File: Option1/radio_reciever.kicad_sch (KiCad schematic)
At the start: 13 parts, among them J3 Conn_01x05_Pin, J4 Conn_01x04_Pin, J5 Conn_01x05_Pin, SW401 4*4*1.7

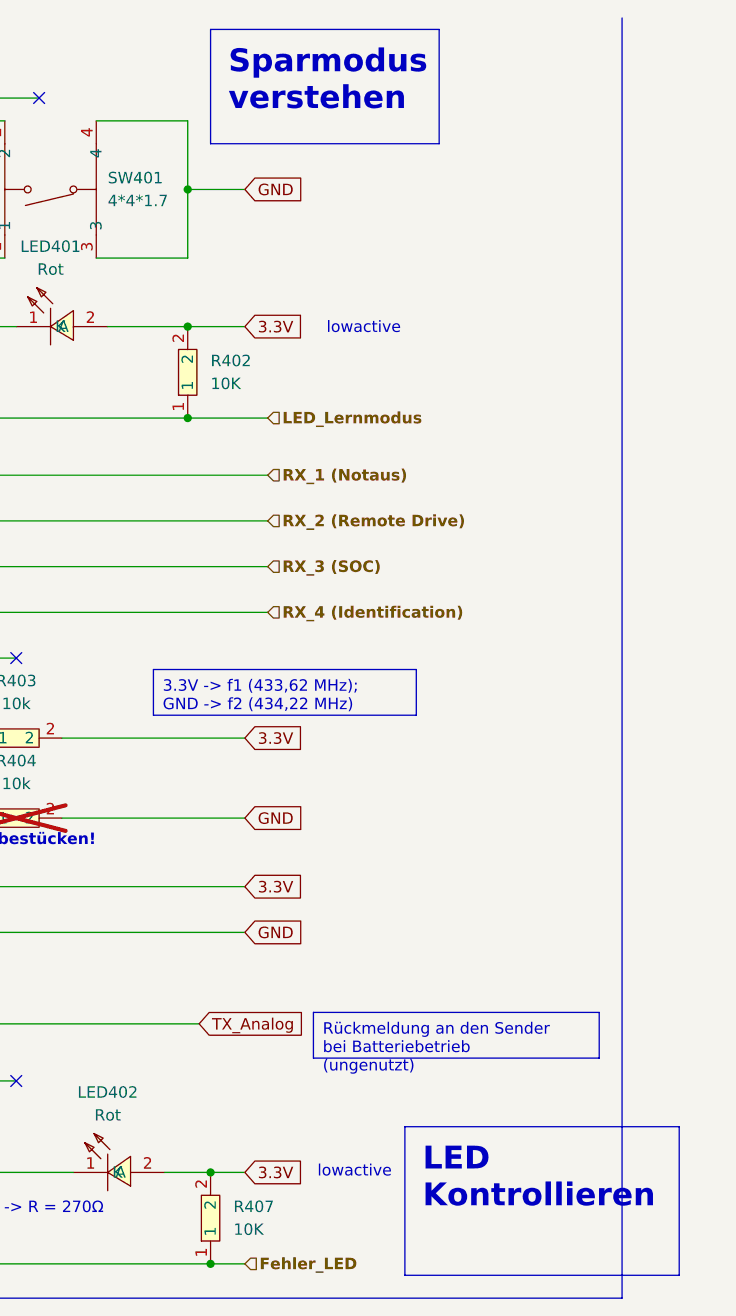
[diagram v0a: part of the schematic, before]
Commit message: SPI Flash hinzugefügt, IN/Outputs vereinheitlicht, USB Flash Möglichkeit hinzugefügt, Display fehtl noch
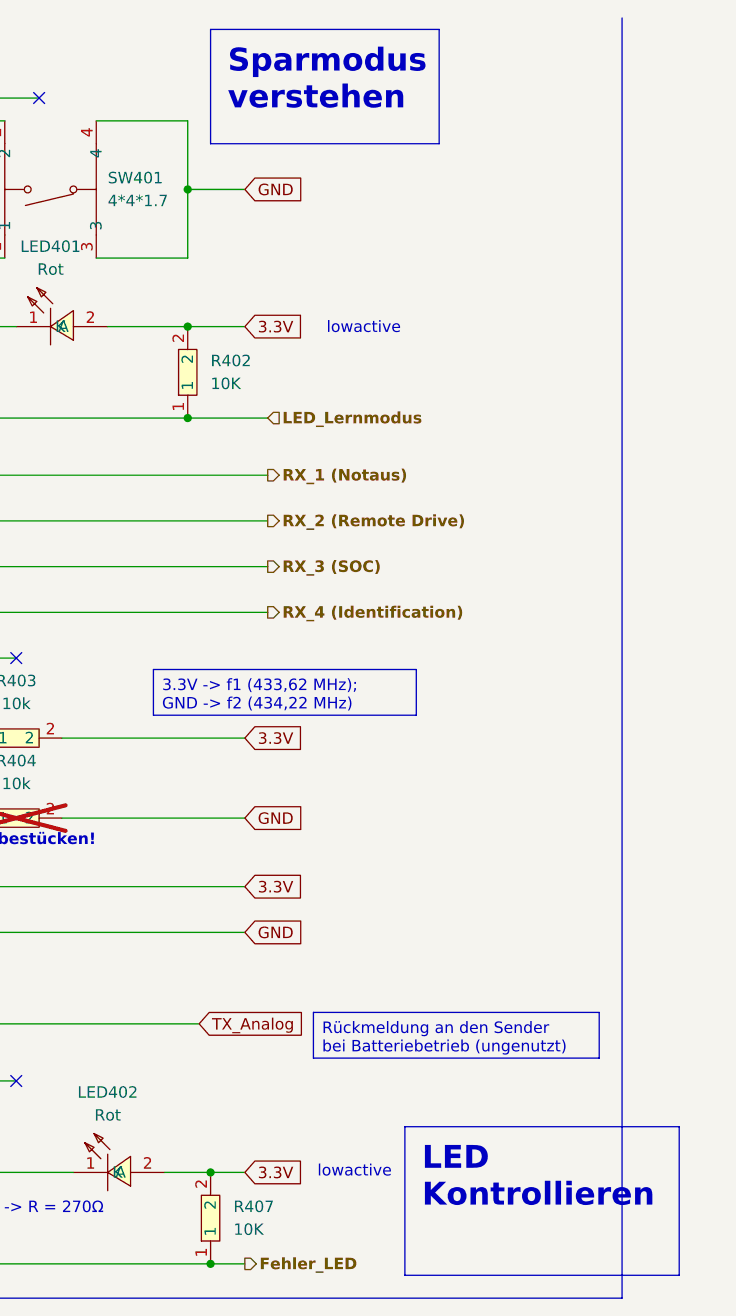
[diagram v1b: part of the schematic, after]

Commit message: Erste issues eingearbeitet
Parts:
- removed LED401, LED402: Rot, easyeda2kicad:LED0603-RD, symbol easyeda2kicad:KT-0603R
- removed R401, R406: 270, easyeda2kicad:R0603, symbol easyeda2kicad:0603WAF2700T5E
- added LED_Error, LED_Learn: XL-1608SYGC-06, easyeda2kicad:LED0603-RD_GREEN, symbol EasyEda2KiCad:XL-1608SYGC-06
- added R401, R406: 220Ω, easyeda2kicad:R0603, symbol EasyEda2KiCad:0603WAJ0221T5E
- R404: now left out of the parts list
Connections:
- net 3.3V: now also LED_Error.2 (A), LED_Learn.2 (A)
- net Fehler_LED: now also R406.1
- net LED_Modus: now also R401.1
- new net: LED_Learn.1 (K), R401.2
- new net: LED_Error.1 (K), R406.2
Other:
- note added: "I_LED = 5mA"
- note removed: "I_LED = 5mA -> R = 270Ω"

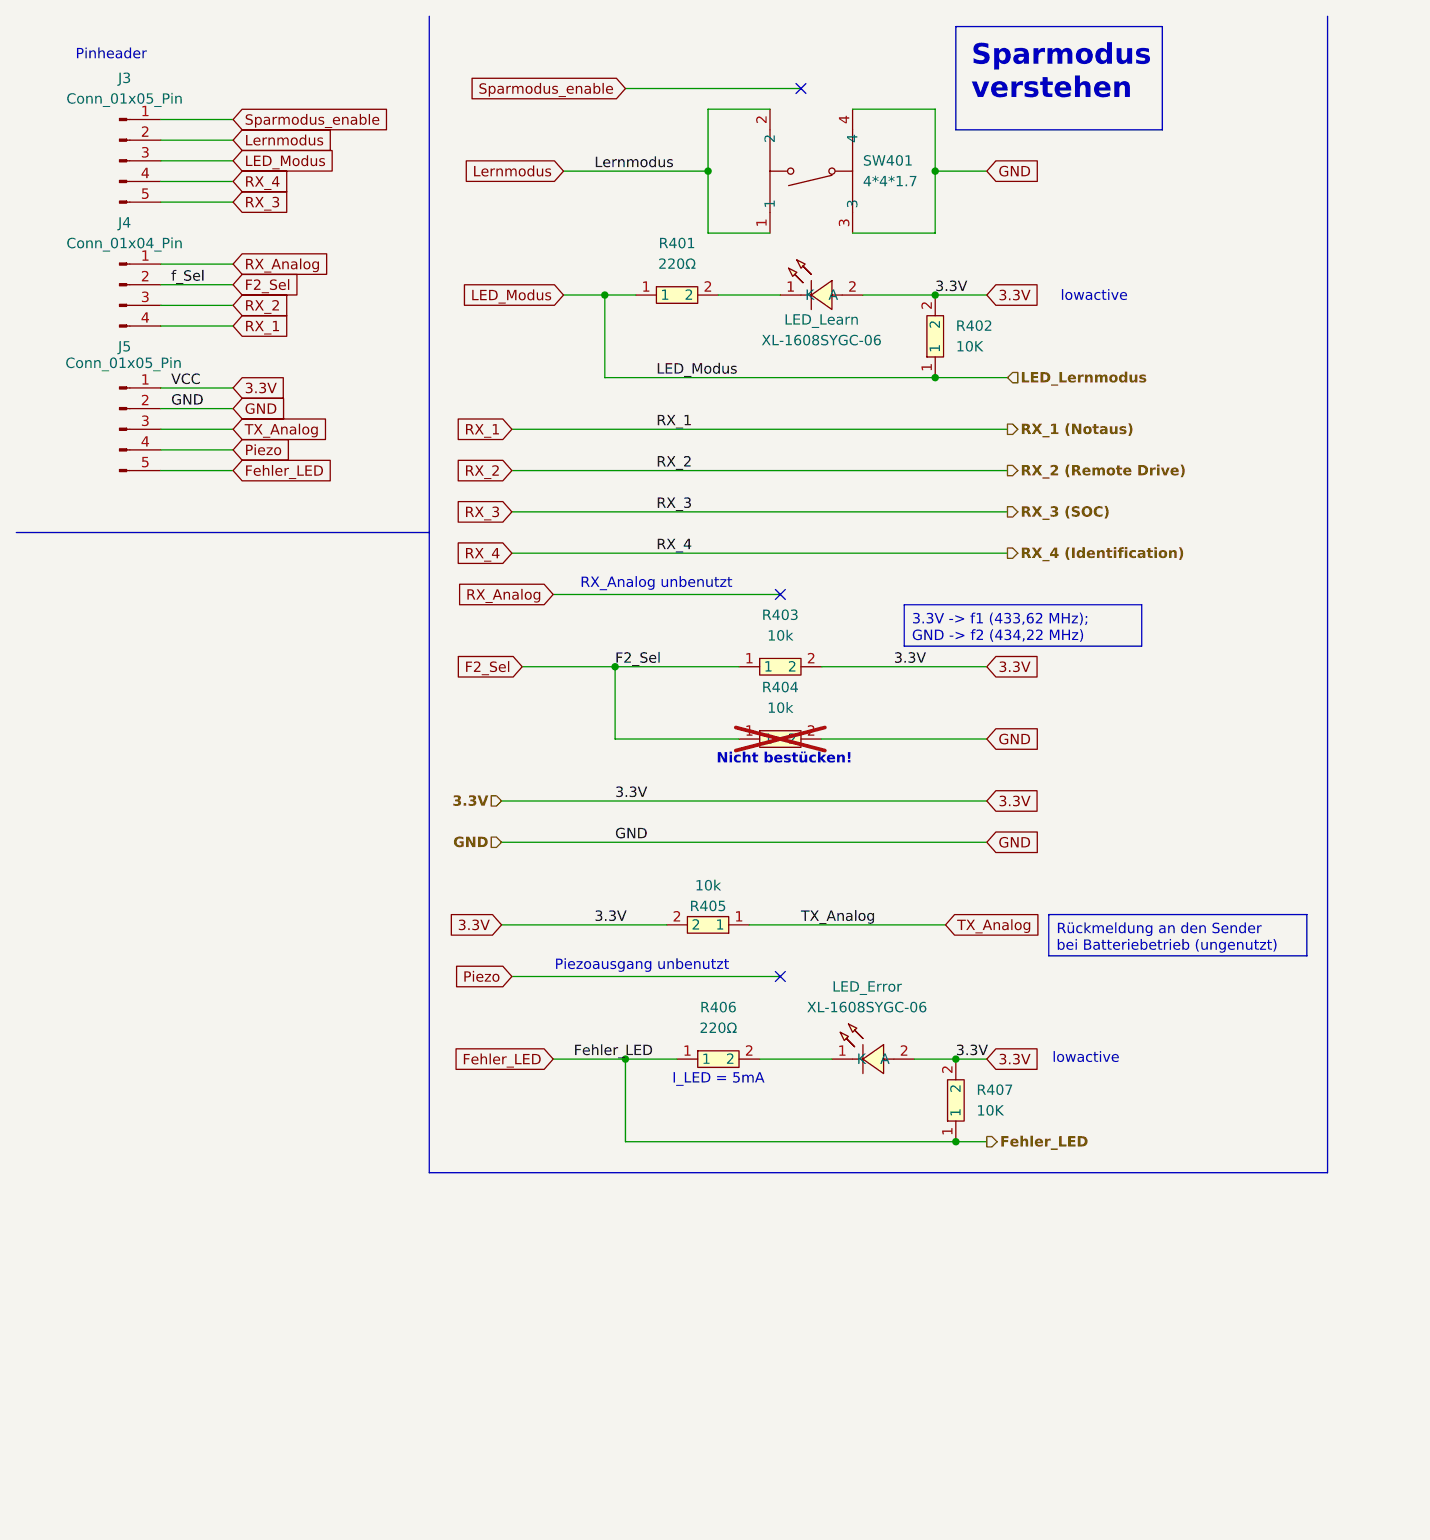
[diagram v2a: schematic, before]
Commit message: USB Schaltung angepasst, Transistoren korrigiert, Stecker ausgetauscht, Dioden hinzugefügt
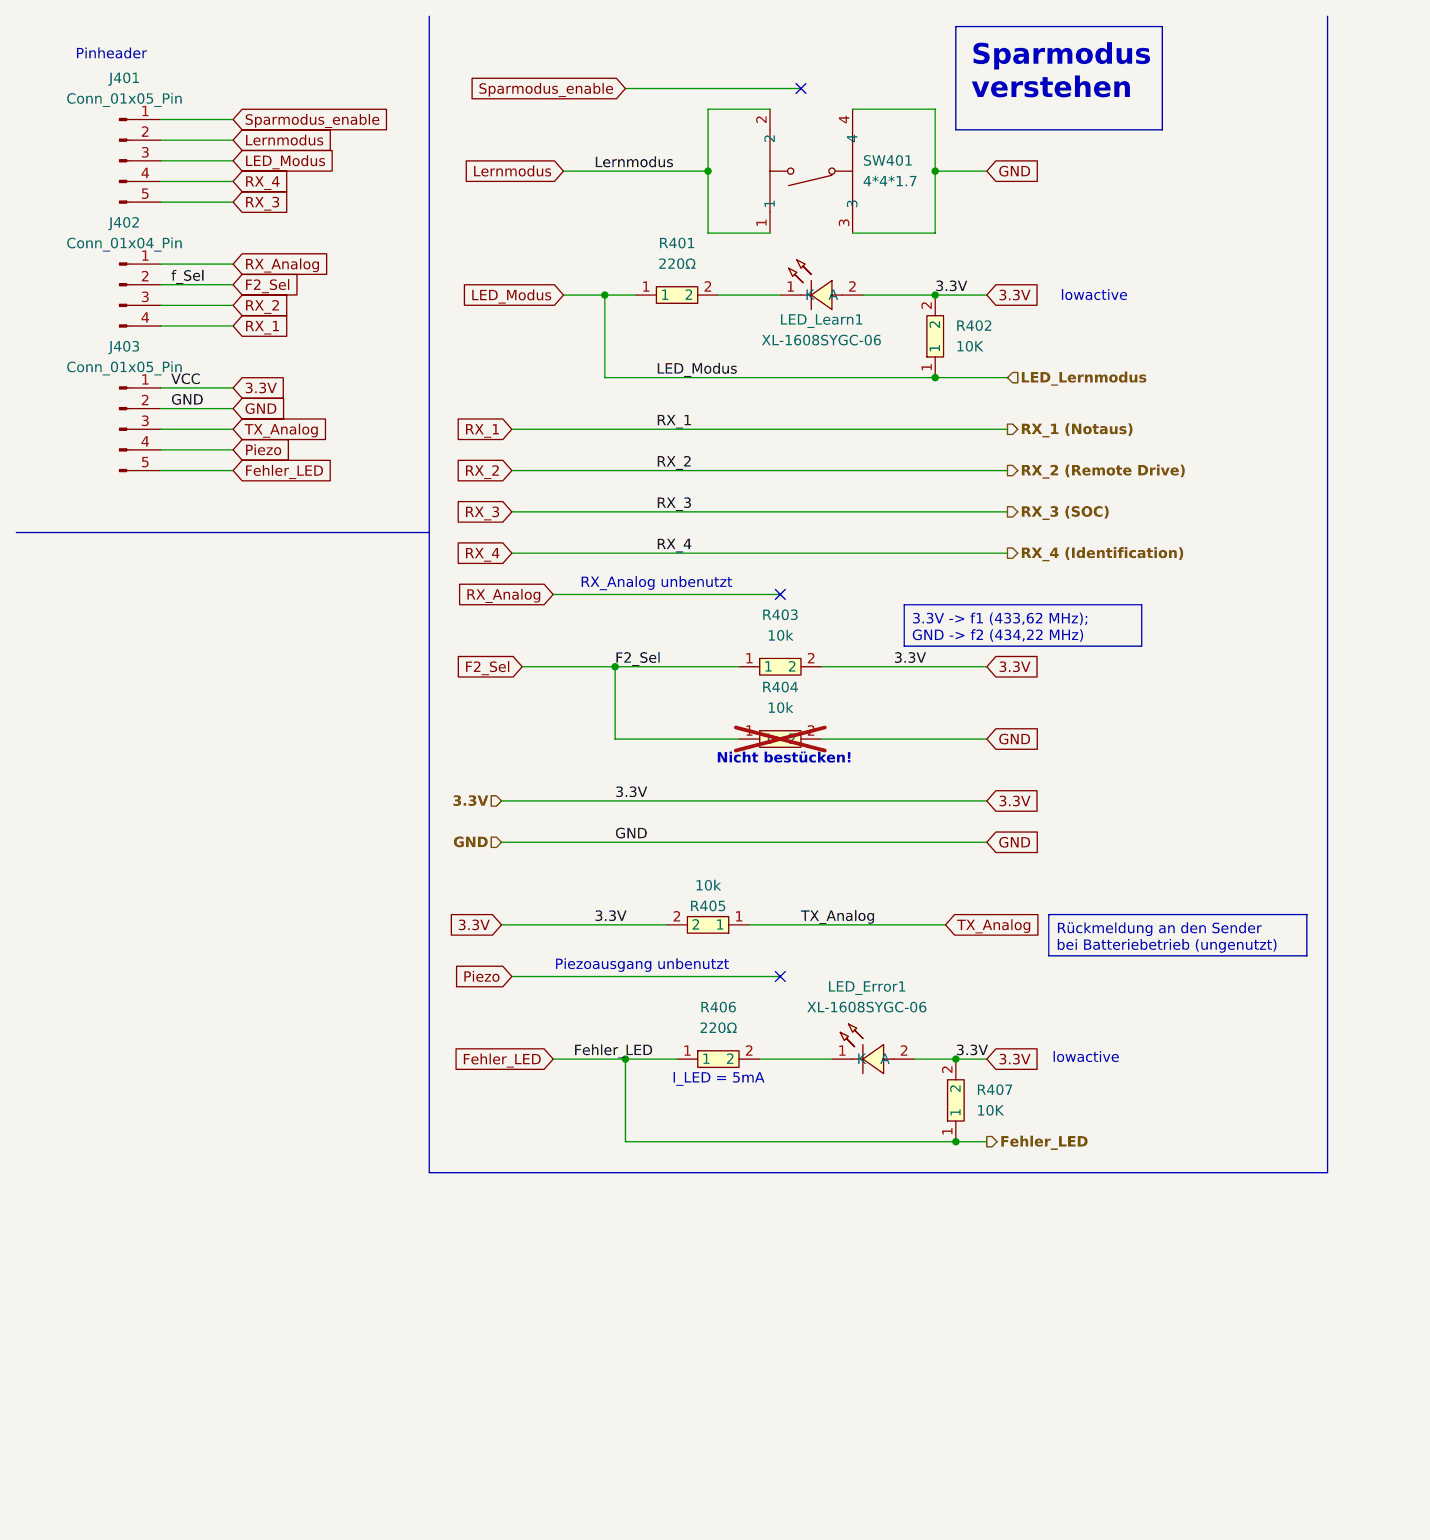
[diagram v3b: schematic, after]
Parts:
- removed J5: Conn_01x05_Pin, symbol Connector:Conn_01x05_Pin
- added J403: Conn_01x05_Pin, Connector_PinHeader_2.54mm:PinHeader_1x05_P2.54mm_Vertical, symbol Connector:Conn_01x05_Pin
- renumbered J3 to J401, J4 to J402, LED_Error to LED_Error1, LED_Learn to LED_Learn1
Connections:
- net 3.3V: now also J403.1 (Pin_1)
- net Fehler_LED: now also J403.5 (Pin_5)
- net GND: now also J403.2 (Pin_2)
- net Piezo: now also J403.4 (Pin_4)
- net TX_Analog: now also J403.3 (Pin_3)

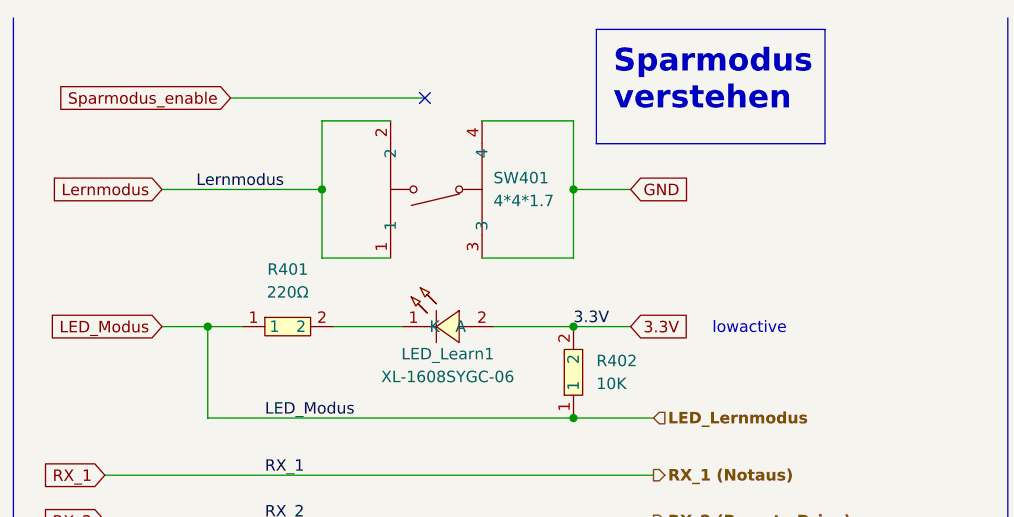
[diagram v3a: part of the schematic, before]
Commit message: EasyEDA Lib in Projekt verschoben; Footprints, Silkscreen für designrule angepasst; Bauteilbeschriftungen entfernt, müssen neu angeordnet werden, JLC Rules eingebunden, Designrules erfolgreich bis auf Beschriftungen, Fehler in Radio Controll Beschaltung behoben; RFID Pinheader hinzugefügt
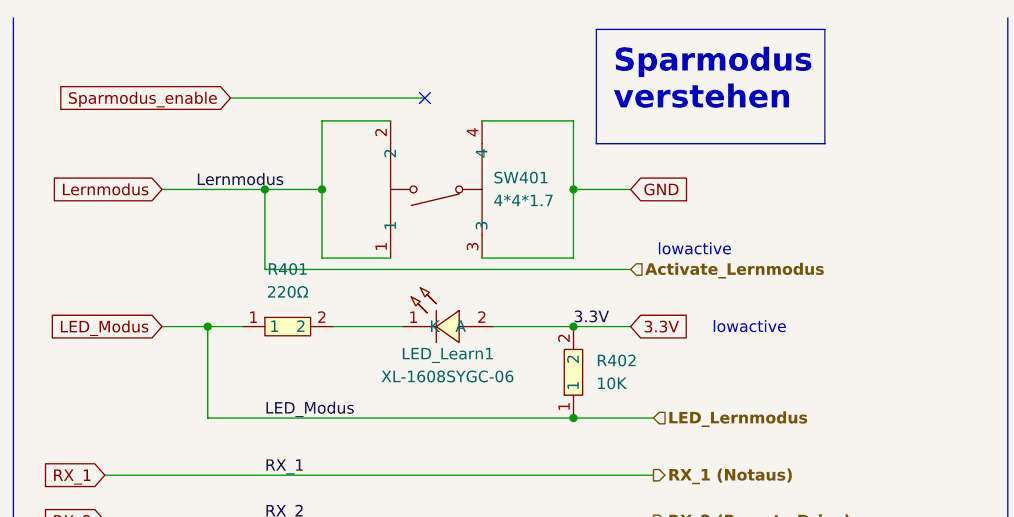
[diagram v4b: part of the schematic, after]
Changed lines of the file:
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@@
+	(text "lowactive"
+		(exclude_from_sim no)
+		(at 139.192 38.608 0)
+		(effects
+			(font
+				(size 1.27 1.27)
+			)
+		)
+	)
 	(text "lowactive"
 		(exclude_from_sim no)
@@
 	)
 	(junction
+		(at 91.44 31.75)
+		(diameter 0)
+		(color 0 0 0 0)
+	)
+	(junction
 		(at 125.73 31.75)
 		(diameter 0)
@@
 	(wire
 		(pts
-			(xy 80.01 31.75) (xy 97.79 31.75)
+			(xy 80.01 31.75) (xy 91.44 31.75)
 		)
 		(stroke
@@
 	(wire
 		(pts
+			(xy 132.08 40.64) (xy 91.44 40.64)
+		)
+		(stroke
+			(width 0)
+			(type default)
+		)
+	)
+	(wire
+		(pts
 			(xy 111.76 101.6) (xy 132.08 101.6)
 		)
@@
 	(wire
 		(pts
+			(xy 91.44 31.75) (xy 97.79 31.75)
+		)
+		(stroke
+			(width 0)
+			(type default)
+		)
+	)
+	(wire
+		(pts
 			(xy 97.79 24.13) (xy 97.79 31.75)
 		)
@@
 		(pts
 			(xy 87.63 140.97) (xy 93.98 140.97)
+		)
+		(stroke
+			(width 0)
+			(type default)
+		)
+	)
+	(wire
+		(pts
+			(xy 91.44 40.64) (xy 91.44 31.75)
 		)
 		(stroke
@@
 		)
 	)
+	(hierarchical_label "Activate_Lernmodus"
+		(shape input)
+		(at 132.08 40.64 0)
+		(effects
+			(font
+				(size 1.27 1.27)
+				(thickness 0.254)
+				(bold yes)
+			)
+			(justify left)
+		)
+	)
